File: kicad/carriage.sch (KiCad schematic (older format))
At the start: 49 parts, among them CON10 Stepstick_Left_Connector, CON11 Stepstick_Right_Connector, CON12 Stepstick_Left_Connector, CON13 Stepstick_Right_Connector, CON19 Stepstick_Left_Connector, CON20 Stepstick_Right_Connector, CON9 Carriage, Q1 IRLR2905ZPBF, Q2 IRLR2905ZPBF, Q3 FDC6401N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

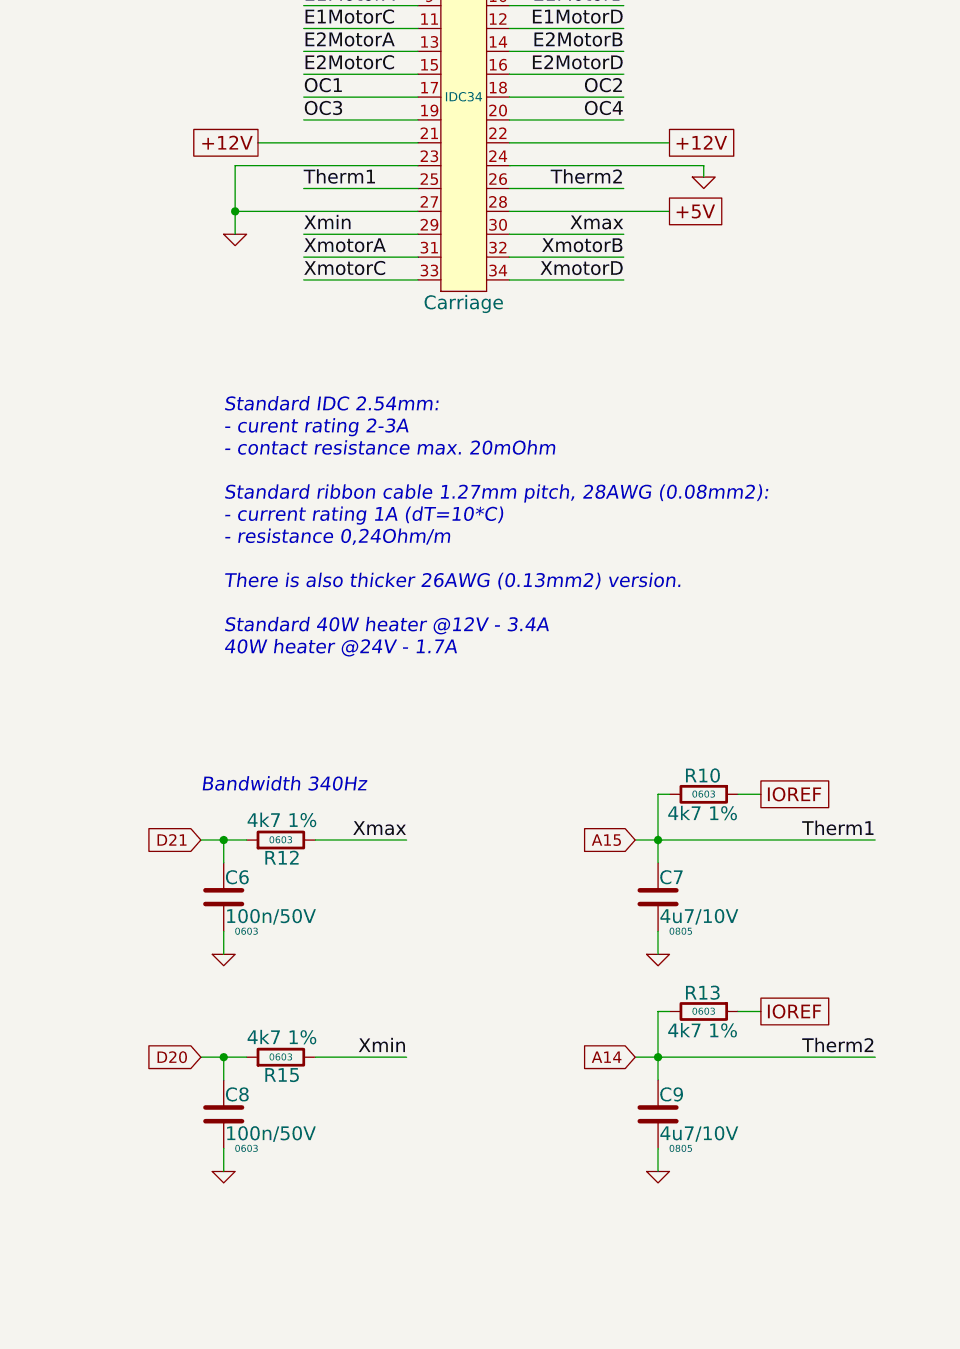
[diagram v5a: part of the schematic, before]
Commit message: Add AGND. Route.
close #27
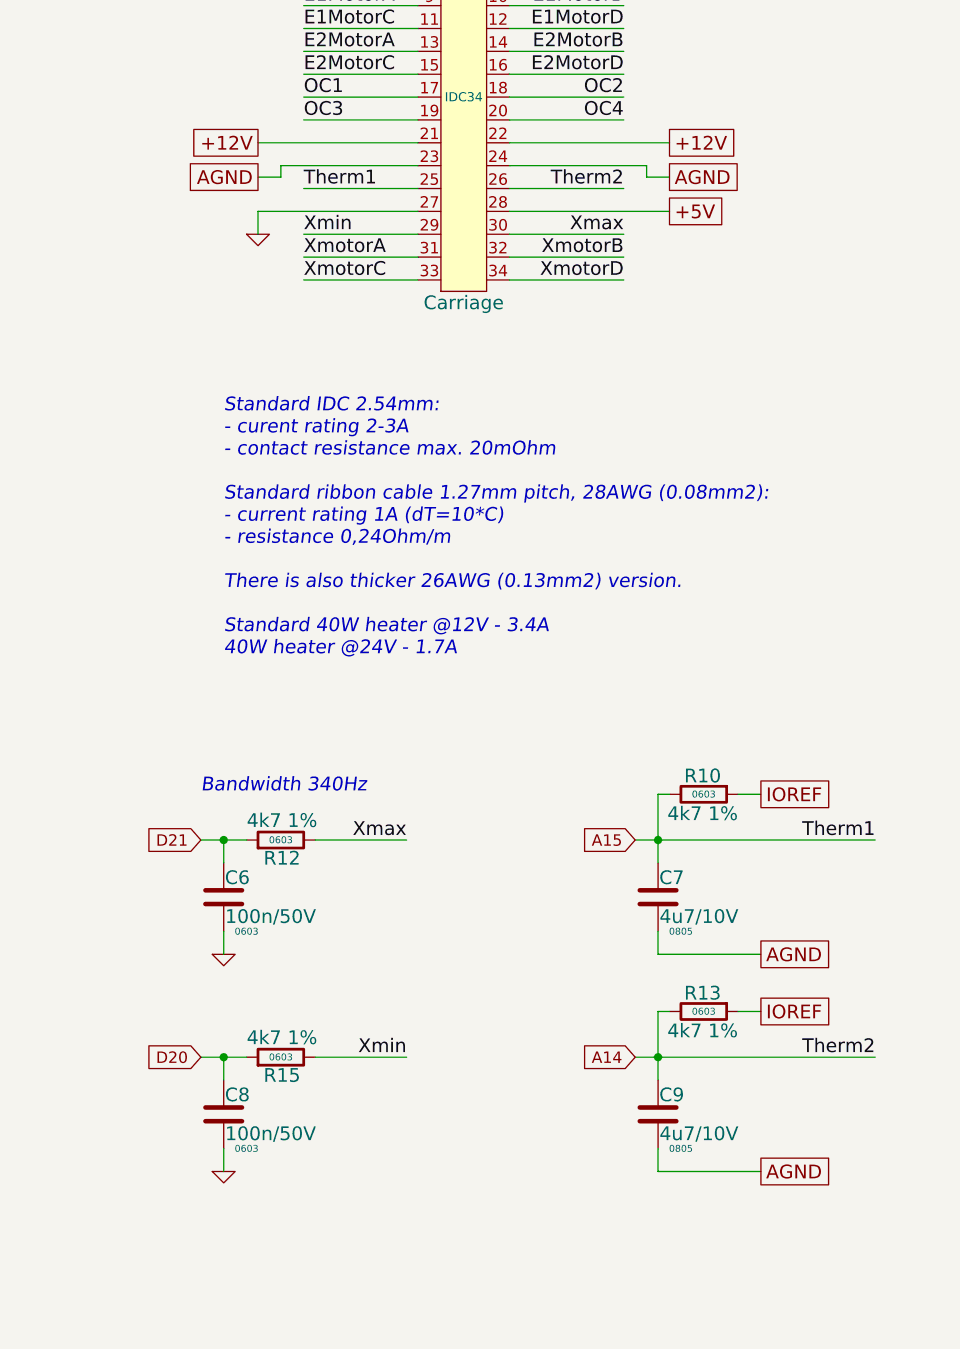
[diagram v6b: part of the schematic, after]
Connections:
- net GND: no longer C7.2, C9.2, CON9.23, CON9.24
- new net AGND: C7.2, C9.2, CON9.23, CON9.24
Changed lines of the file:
@@
 A12
 $Comp
-L GND #PWR04
+L GND #PWR02
 U 1 1 534C44E8
 P 6050 3950
-F 0 "#PWR04" H 6050 3950 30  0001 C CNN
+F 0 "#PWR02" H 6050 3950 30  0001 C CNN
 F 1 "GND" H 6050 3880 30  0001 C CNN
 F 2 "~" H 6050 3950 60  0000 C CNN
@@
 D9
 $Comp
-L GND #PWR05
+L GND #PWR03
 U 1 1 534D96C2
 P 6050 2100
-F 0 "#PWR05" H 6050 2100 30  0001 C CNN
+F 0 "#PWR03" H 6050 2100 30  0001 C CNN
 F 1 "GND" H 6050 2030 30  0001 C CNN
 F 2 "~" H 6050 2100 60  0000 C CNN
@@
 D10
 $Comp
-L GND #PWR06
+L GND #PWR04
 U 1 1 534D96EE
 P 4750 2100
-F 0 "#PWR06" H 4750 2100 30  0001 C CNN
+F 0 "#PWR04" H 4750 2100 30  0001 C CNN
 F 1 "GND" H 4750 2030 30  0001 C CNN
 F 2 "~" H 4750 2100 60  0000 C CNN
@@
 	1    0    0    -1
 $EndComp
-$Comp
-L GND #PWR07
-U 1 1 534EDD0C
-P 9650 5350
-F 0 "#PWR07" H 9650 5350 30  0001 C CNN
-F 1 "GND" H 9650 5280 30  0001 C CNN
-F 2 "~" H 9650 5350 60  0000 C CNN
-F 3 "~" H 9650 5350 60  0000 C CNN
-	1    9650 5350
-	1    0    0    -1
-$EndComp
 Text GLabel 9550 4850 0    50   Input ~ 0
 A15
-$Comp
-L GND #PWR08
-U 1 1 534EDD2B
-P 9650 6300
-F 0 "#PWR08" H 9650 6300 30  0001 C CNN
-F 1 "GND" H 9650 6230 30  0001 C CNN
-F 2 "~" H 9650 6300 60  0000 C CNN
-F 3 "~" H 9650 6300 60  0000 C CNN
-	1    9650 6300
-	1    0    0    -1
-$EndComp
 Text GLabel 9550 5800 0    50   Input ~ 0
 A14
@@
 Text GLabel 9700 1800 2    60   UnSpc ~ 0
 +12V
-$Comp
-L GND #PWR09
-U 1 1 536FC9C8
-P 7800 2200
-F 0 "#PWR09" H 7800 2200 30  0001 C CNN
-F 1 "GND" H 7800 2130 30  0001 C CNN
-F 2 "~" H 7800 2200 60  0000 C CNN
-F 3 "~" H 7800 2200 60  0000 C CNN
-	1    7800 2200
-	1    0    0    -1
-$EndComp
-$Comp
-L GND #PWR010
-U 1 1 536FC9D3
-P 9850 1950
-F 0 "#PWR010" H 9850 1950 30  0001 C CNN
-F 1 "GND" H 9850 1880 30  0001 C CNN
-F 2 "~" H 9850 1950 60  0000 C CNN
-F 3 "~" H 9850 1950 60  0000 C CNN
-	1    9850 1950
-	1    0    0    -1
-$EndComp
 Text Label 10600 5800 2    60   ~ 0
 Therm2
@@
 D20
 $Comp
-L GND #PWR011
+L GND #PWR05
 U 1 1 536FECC5
 P 4700 3950
-F 0 "#PWR011" H 4700 3950 30  0001 C CNN
+F 0 "#PWR05" H 4700 3950 30  0001 C CNN
 F 1 "GND" H 4700 3880 30  0001 C CNN
 F 2 "~" H 4700 3950 60  0000 C CNN
@@
 $EndComp
 $Comp
-L GND #PWR012
+L GND #PWR06
 U 1 1 537E69CA
 P 7750 5350
-F 0 "#PWR012" H 7750 5350 30  0001 C CNN
+F 0 "#PWR06" H 7750 5350 30  0001 C CNN
 F 1 "GND" H 7750 5280 30  0001 C CNN
 F 2 "~" H 7750 5350 60  0000 C CNN
@@
 $EndComp
 $Comp
-L GND #PWR013
+L GND #PWR07
 U 1 1 537E6A07
 P 7750 6300
-F 0 "#PWR013" H 7750 6300 30  0001 C CNN
+F 0 "#PWR07" H 7750 6300 30  0001 C CNN
 F 1 "GND" H 7750 6230 30  0001 C CNN
 F 2 "~" H 7750 6300 60  0000 C CNN
@@
 $EndComp
 $Comp
-L GND #PWR014
+L GND #PWR08
 U 1 1 539228B4
 P 4500 5450
-F 0 "#PWR014" H 4500 5450 30  0001 C CNN
+F 0 "#PWR08" H 4500 5450 30  0001 C CNN
 F 1 "GND" H 4500 5380 30  0001 C CNN
 F 2 "~" H 4500 5450 60  0000 C CNN
@@
 $EndComp
 $Comp
-L GND #PWR015
+L GND #PWR09
 U 1 1 53922C93
 P 4500 6800
-F 0 "#PWR015" H 4500 6800 30  0001 C CNN
+F 0 "#PWR09" H 4500 6800 30  0001 C CNN
 F 1 "GND" H 4500 6730 30  0001 C CNN
 F 2 "~" H 4500 6800 60  0000 C CNN
@@
 $EndComp
 $Comp
-L GND #PWR016
+L GND #PWR010
 U 1 1 53922EC9
 P 5800 5450
-F 0 "#PWR016" H 5800 5450 30  0001 C CNN
+F 0 "#PWR010" H 5800 5450 30  0001 C CNN
 F 1 "GND" H 5800 5380 30  0001 C CNN
 F 2 "~" H 5800 5450 60  0000 C CNN
@@
 $EndComp
 $Comp
-L GND #PWR017
+L GND #PWR011
 U 1 1 53922EFB
 P 5800 6800
-F 0 "#PWR017" H 5800 6800 30  0001 C CNN
+F 0 "#PWR011" H 5800 6800 30  0001 C CNN
 F 1 "GND" H 5800 6730 30  0001 C CNN
 F 2 "~" H 5800 6800 60  0000 C CNN
@@
 Wire Wire Line
 	9700 2100 9000 2100
-Connection ~ 7800 2100
-Wire Wire Line
-	7800 1900 7800 2200
-Wire Wire Line
-	9850 1900 9850 1950
 Wire Wire Line
 	9000 2400 9500 2400
@@
 	8100 2200 8600 2200
 Wire Wire Line
-	7800 2100 8600 2100
-Wire Wire Line
 	8100 2000 8600 2000
 Wire Wire Line
-	7800 1900 8600 1900
-Wire Wire Line
 	7900 1800 8600 1800
 Wire Wire Line
@@
 Wire Wire Line
 	9500 2000 9000 2000
-Wire Wire Line
-	9000 1900 9850 1900
 Wire Wire Line
 	9700 1800 9000 1800
@@
 $EndComp
 $Comp
-L GND #PWR018
+L GND #PWR012
 U 1 1 536FB0A2
 P 2900 2500
-F 0 "#PWR018" H 2900 2500 30  0001 C CNN
+F 0 "#PWR012" H 2900 2500 30  0001 C CNN
 F 1 "GND" H 2900 2430 30  0001 C CNN
 F 2 "~" H 2900 2500 60  0000 C CNN
@@
 X
 $Comp
-L GND #PWR019
+L GND #PWR013
 U 1 1 534EC7A1
 P 1700 2500
-F 0 "#PWR019" H 1700 2500 30  0001 C CNN
+F 0 "#PWR013" H 1700 2500 30  0001 C CNN
 F 1 "GND" H 1700 2430 30  0001 C CNN
 F 2 "~" H 1700 2500 60  0000 C CNN
@@
 $EndComp
 $Comp
-L GND #PWR020
+L GND #PWR014
 U 1 1 534EC79B
 P 2700 2500
-F 0 "#PWR020" H 2700 2500 30  0001 C CNN
+F 0 "#PWR014" H 2700 2500 30  0001 C CNN
 F 1 "GND" H 2700 2430 30  0001 C CNN
 F 2 "~" H 2700 2500 60  0000 C CNN
@@
 $EndComp
 $Comp
-L GND #PWR021
+L GND #PWR015
 U 1 1 539A105B
 P 2900 7350
-F 0 "#PWR021" H 2900 7350 30  0001 C CNN
+F 0 "#PWR015" H 2900 7350 30  0001 C CNN
 F 1 "GND" H 2900 7280 30  0001 C CNN
 F 2 "~" H 2900 7350 60  0000 C CNN
@@
 E2
 $Comp
-L GND #PWR022
+L GND #PWR016
 U 1 1 539A1070
 P 1700 7350
-F 0 "#PWR022" H 1700 7350 30  0001 C CNN
+F 0 "#PWR016" H 1700 7350 30  0001 C CNN
 F 1 "GND" H 1700 7280 30  0001 C CNN
 F 2 "~" H 1700 7350 60  0000 C CNN
@@
 $EndComp
 $Comp
-L GND #PWR023
+L GND #PWR017
 U 1 1 539A1076
 P 2700 7350
-F 0 "#PWR023" H 2700 7350 30  0001 C CNN
+F 0 "#PWR017" H 2700 7350 30  0001 C CNN
 F 1 "GND" H 2700 7280 30  0001 C CNN
 F 2 "~" H 2700 7350 60  0000 C CNN
@@
 	4050 6150 4050 6200
 $Comp
-L GND #PWR024
+L GND #PWR018
 U 1 1 539D1289
 P 4050 6200
-F 0 "#PWR024" H 4050 6200 30  0001 C CNN
+F 0 "#PWR018" H 4050 6200 30  0001 C CNN
 F 1 "GND" H 4050 6130 30  0001 C CNN
 F 2 "~" H 4050 6200 60  0000 C CNN
@@
 	3950 4800 3950 4850
 $Comp
-L GND #PWR025
+L GND #PWR019
 U 1 1 539D12FB
 P 3950 4850
-F 0 "#PWR025" H 3950 4850 30  0001 C CNN
+F 0 "#PWR019" H 3950 4850 30  0001 C CNN
 F 1 "GND" H 3950 4780 30  0001 C CNN
 F 2 "~" H 3950 4850 60  0000 C CNN
@@
 Stepper Driver
 $Comp
-L GND #PWR026
+L GND #PWR020
 U 1 1 53A8D4D7
 P 2700 4950
-F 0 "#PWR026" H 2700 4950 30  0001 C CNN
+F 0 "#PWR020" H 2700 4950 30  0001 C CNN
 F 1 "GND" H 2700 4880 30  0001 C CNN
 F 2 "~" H 2700 4950 60  0000 C CNN
@@
 $EndComp
 $Comp
-L GND #PWR027
+L GND #PWR021
 U 1 1 53A8D4DD
 P 1700 4950
-F 0 "#PWR027" H 1700 4950 30  0001 C CNN
+F 0 "#PWR021" H 1700 4950 30  0001 C CNN
 F 1 "GND" H 1700 4880 30  0001 C CNN
 F 2 "~" H 1700 4950 60  0000 C CNN
@@
 $EndComp
 $Comp
-L GND #PWR028
+L GND #PWR022
 U 1 1 53A8D4F2
 P 2900 4950
-F 0 "#PWR028" H 2900 4950 30  0001 C CNN
+F 0 "#PWR022" H 2900 4950 30  0001 C CNN
 F 1 "GND" H 2900 4880 30  0001 C CNN
 F 2 "~" H 2900 4950 60  0000 C CNN
@@
 Text GLabel 1000 3650 0    50   Input ~ 0
 A0
+Text GLabel 10100 5350 2    60   UnSpc ~ 0
+AGND
+Wire Wire Line
+	10100 5350 9650 5350
+Text GLabel 10100 6300 2    60   UnSpc ~ 0
+AGND
+Wire Wire Line
+	10100 6300 9650 6300
+Wire Wire Line
+	9000 1900 9600 1900
+Wire Wire Line
+	9600 1900 9600 1950
+Wire Wire Line
+	9600 1950 9700 1950
+Text GLabel 9700 1950 2    60   UnSpc ~ 0
+AGND
+Wire Wire Line
+	8600 1900 8000 1900
+Wire Wire Line
+	7900 2100 8600 2100
+Text GLabel 7900 1950 0    60   UnSpc ~ 0
+AGND
+Wire Wire Line
+	7900 2100 7900 2200
+$Comp
+L GND #PWR023
+U 1 1 53A93123
+P 7900 2200
+F 0 "#PWR023" H 7900 2200 30  0001 C CNN
+F 1 "GND" H 7900 2130 30  0001 C CNN
+F 2 "~" H 7900 2200 60  0000 C CNN
+F 3 "~" H 7900 2200 60  0000 C CNN
+	1    7900 2200
+	1    0    0    -1
+$EndComp
+Wire Wire Line
+	7900 1950 8000 1950
+Wire Wire Line
+	8000 1950 8000 1900
 $EndSCHEMATC

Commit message: Route.
Routed board with some minor DRC issues.
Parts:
- removed C24: 100n/50V, 0603, symbol C
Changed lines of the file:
@@
 	4500 4400 4500 4500
-Wire Wire Line
-	3950 4400 4600 4400
 Wire Wire Line
 	5800 4400 5800 4500
@@
 $EndComp
 $Comp
-L C C24
-U 1 1 539D12F3
-P 3950 4650
-F 0 "C24" H 3955 4735 60  0000 L CNN
-F 1 "100n/50V" H 3956 4565 60  0000 L CNN
-F 2 "0603" H 4050 4500 30  0000 C CNN
-F 3 "~" H 3950 4650 60  0000 C CNN
-	1    3950 4650
-	-1   0    0    -1
-$EndComp
-Wire Wire Line
-	3950 4400 3950 4500
-Wire Wire Line
-	3950 4800 3950 4850
-$Comp
-L GND #PWR019
-U 1 1 539D12FB
-P 3950 4850
-F 0 "#PWR019" H 3950 4850 30  0001 C CNN
-F 1 "GND" H 3950 4780 30  0001 C CNN
-F 2 "~" H 3950 4850 60  0000 C CNN
-F 3 "~" H 3950 4850 60  0000 C CNN
-	1    3950 4850
-	1    0    0    -1
-$EndComp
-Connection ~ 4500 4400
-$Comp
 L stepstickFootprint MECH6
 U 1 1 53A8D4CF
@@
 Stepper Driver
 $Comp
-L GND #PWR020
+L GND #PWR019
 U 1 1 53A8D4D7
 P 2700 4950
-F 0 "#PWR020" H 2700 4950 30  0001 C CNN
+F 0 "#PWR019" H 2700 4950 30  0001 C CNN
 F 1 "GND" H 2700 4880 30  0001 C CNN
 F 2 "~" H 2700 4950 60  0000 C CNN
@@
 $EndComp
 $Comp
-L GND #PWR021
+L GND #PWR020
 U 1 1 53A8D4DD
 P 1700 4950
-F 0 "#PWR021" H 1700 4950 30  0001 C CNN
+F 0 "#PWR020" H 1700 4950 30  0001 C CNN
 F 1 "GND" H 1700 4880 30  0001 C CNN
 F 2 "~" H 1700 4950 60  0000 C CNN
@@
 $EndComp
 $Comp
-L GND #PWR022
+L GND #PWR021
 U 1 1 53A8D4F2
 P 2900 4950
-F 0 "#PWR022" H 2900 4950 30  0001 C CNN
+F 0 "#PWR021" H 2900 4950 30  0001 C CNN
 F 1 "GND" H 2900 4880 30  0001 C CNN
 F 2 "~" H 2900 4950 60  0000 C CNN
@@
 	7900 2100 7900 2200
 $Comp
-L GND #PWR023
+L GND #PWR022
 U 1 1 53A93123
 P 7900 2200
-F 0 "#PWR023" H 7900 2200 30  0001 C CNN
+F 0 "#PWR022" H 7900 2200 30  0001 C CNN
 F 1 "GND" H 7900 2130 30  0001 C CNN
 F 2 "~" H 7900 2200 60  0000 C CNN
@@
 Wire Wire Line
 	8000 1950 8000 1900
+Wire Wire Line
+	4500 4400 4600 4400
 $EndSCHEMATC
